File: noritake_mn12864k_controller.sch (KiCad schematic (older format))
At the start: 43 parts, among them J1 Conn_01x11, J2 USB_C_Receptacle_USB2.0, J3 TagConnect_TC2030_SWD, Q1 AO3400A, Q2 AO3400A, T1 Wuerth 760390013, U1 MN12864K, U2 74HC14, U3 CD4051B, U4 SN74AVC8T245PW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

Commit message: Connect shutdown and ifsel
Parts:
- removed C12, C3, C4: 100nF, Capacitor_SMD:C_0402_1005Metric, symbol Device:C
- removed C24: 10uF, Capacitor_SMD:C_1206_3216Metric, symbol Device:C
- removed C25: 4.7uF, Capacitor_SMD:C_1206_3216Metric, symbol Device:C
- removed C?: 1uF, Capacitor_SMD:C_0402_1005Metric, symbol Device:C
- removed D1: 5V6, Diode_SMD:D_MiniMELF, symbol Device:D_Zener
- removed Q1, Q2: AO3400A, Package_TO_SOT_SMD:SOT-23, symbol Transistor_FET:AO3400A
- removed R5: 22R, Resistor_SMD:R_1206_3216Metric, symbol Device:R
- removed R7: 10kR, Resistor_SMD:R_1206_3216Metric, symbol Device:R
- removed T1: Wuerth 760390013, Transformer_Würth:Transformer_Würth_10.05x6.73_6P, symbol Transformer_Isolation:Transformer_SP_SS
- removed U1: MN12864K, VFD_Noritake:MN12864K, symbol VFD_Noritake:MN12864K
- removed U4: SN74AVC8T245PW, Package_SO:TSSOP-24_4.4x7.8mm_P0.65mm, symbol Logic_LevelTranslator:SN74AVC8T245PW
- added H1, H2: ToolingHole, ToolingHole:ToolingHole_JLCSMT, symbol Mechanical:MountingHole
- added H3, H4: MountingHole, MountingHole:MountingHole_2.7mm_M2.5, symbol Mechanical:MountingHole
- added R? (x4): 100kR, Resistor_SMD:R_0402_1005Metric, symbol Device:R
- added TP1: DEBUG00, TestPoint:TestPoint_Pad_D2.0mm, symbol Connector:TestPoint
- added TP?: DEBUG01, TestPoint:TestPoint_Pad_D2.0mm, symbol Connector:TestPoint
- added TP?: DEBUG02, TestPoint:TestPoint_Pad_D2.0mm, symbol Connector:TestPoint
- added TP?: DEBUG03, TestPoint:TestPoint_Pad_D2.0mm, symbol Connector:TestPoint
- added TP?: DEBUG04, TestPoint:TestPoint_Pad_D2.0mm, symbol Connector:TestPoint
- added TP?: DEBUG05, TestPoint:TestPoint_Pad_D2.0mm, symbol Connector:TestPoint
- added TP?: DEBUG06, TestPoint:TestPoint_Pad_D2.0mm, symbol Connector:TestPoint
- added TP?: DEBUG07, TestPoint:TestPoint_Pad_D2.0mm, symbol Connector:TestPoint
- added TP?: DEBUG08, TestPoint:TestPoint_Pad_D2.0mm, symbol Connector:TestPoint
- added TP?: DEBUG09, TestPoint:TestPoint_Pad_D2.0mm, symbol Connector:TestPoint
- added TP?: DEBUG10, TestPoint:TestPoint_Pad_D2.0mm, symbol Connector:TestPoint
- added TP?: DEBUG11, TestPoint:TestPoint_Pad_D2.0mm, symbol Connector:TestPoint
- added TP?: DEBUG12, TestPoint:TestPoint_Pad_D2.0mm, symbol Connector:TestPoint
- added TP?: DEBUG13, TestPoint:TestPoint_Pad_D2.0mm, symbol Connector:TestPoint
- added TP?: DEBUG14, TestPoint:TestPoint_Pad_D2.0mm, symbol Connector:TestPoint
- added TP?: DEBUG15, TestPoint:TestPoint_Pad_D2.0mm, symbol Connector:TestPoint
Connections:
- net +3V3: now also R?.1, R?.1, R?.2, R?.2
- net CPOL: now also J1.3 (Pin_3); no longer J1.5 (Pin_5)
- net IFSEL: now also U5.56 (PB4), R?.1
- net VFD_BLK: now also U5.25 (PB0); no longer U5.50 (PA15)
- net VFD_GSBLK: now also U5.26 (PB1); no longer U5.42 (PA9)
- net VFD_LAT: now also U5.42 (PA9); no longer U5.41 (PA8)
- net ~CS: now also R?.2
- net ~RST: now also J1.5 (Pin_5), R?.2; no longer J1.3 (Pin_3)
- net ~SHDWN: now also U5.58 (PB6), R?.1
- net DBG08: now reaches U5.10 (PC2)
- net DBG08: now also TP?.1
- net DBG09: now reaches U5.11 (PC3)
- net DBG09: now also TP?.1
- net DBG10: now reaches U5.24 (PC4)
- net DBG10: now also TP?.1
- net DBG05: now reaches U5.27 (PB2)
- net DBG05: now also TP?.1
- net DBG01: now reaches U5.28 (PB10)
- net DBG01: now also TP?.1
- net DBG02: now reaches U5.29 (PB11)
- net DBG02: now also TP?.1
- net DBG03: now reaches U5.33 (PB12)
- net DBG03: now also TP?.1
- net DBG04: now reaches U5.35 (PB14)
- net DBG04: now also TP?.1
- net DBG11: now reaches U5.37 (PC6)
- net DBG11: now also TP?.1
- net DBG12: now reaches U5.38 (PC7)
- net DBG12: now also TP?.1
- net DBG13: now reaches U5.39 (PC8)
- net DBG13: now also TP?.1
- net DBG14: now reaches U5.40 (PC9)
- net DBG14: now also TP?.1
- net VFD_HTR_G2: now reaches U5.43 (PA10)
- net DBG15: now reaches U5.51 (PC10)
- net DBG15: now also TP?.1
- net DBG00: now reaches U5.62 (PB9)
- net DBG00: now also TP1.1
- net DBG06: now reaches U5.8 (PC0)
- net DBG06: now also TP?.1
- net DBG07: now reaches U5.9 (PC1)
- net DBG07: now also TP?.1
- new net VFD_HTR_G1: U5.41 (PA8)
- new net VFD_HV_EN: U5.50 (PA15)
- no-connect marks 8 -> 7
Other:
- moved on the sheet: C15, C16, C17, C19, C20, C22, C23, J3, JP1, R6, U5

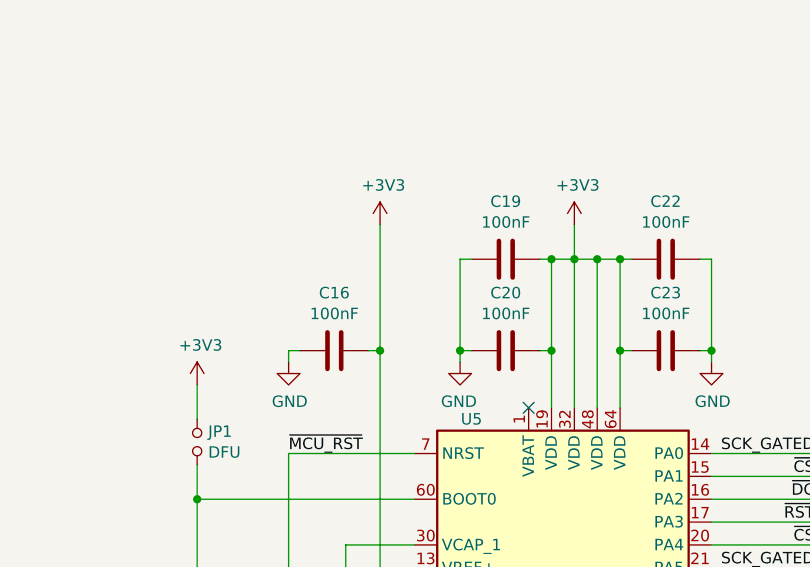
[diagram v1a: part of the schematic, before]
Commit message: Add dual filament transformer option
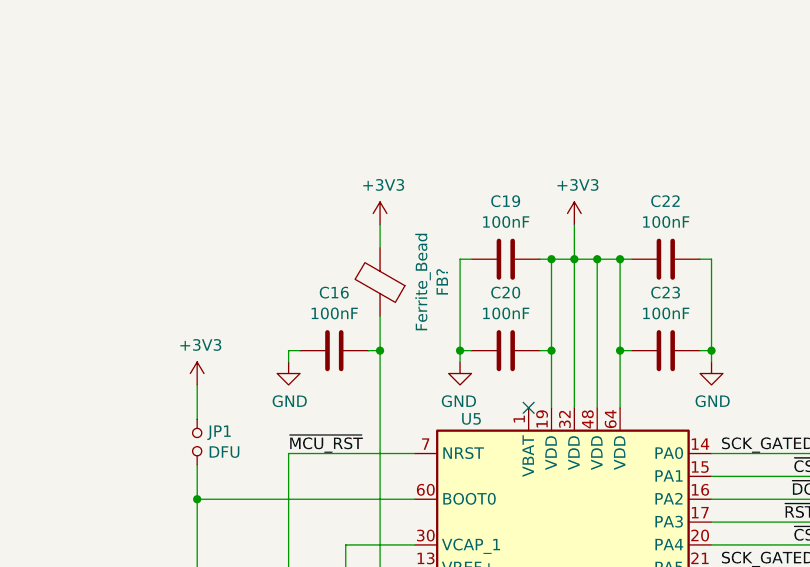
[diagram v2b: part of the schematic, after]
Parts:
- added FB?: Ferrite_Bead, Inductor_SMD:L_0805_2012Metric, symbol Device:Ferrite_Bead
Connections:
- net +3V3: now also FB?.2; no longer C16.2, U5.13 (VREF+)
- new net: C16.2, FB?.1, U5.13 (VREF+)
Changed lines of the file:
@@
 Wire Wire Line
 	14850 4000 14900 4000
-Connection ~ 14900 4000
-Wire Wire Line
-	14900 4000 14900 3450
 Wire Wire Line
 	15050 4850 14750 4850
@@
 Text Label 16800 6750 2    50   ~ 0
 ~SHDWN
+$Comp
+L Device:Ferrite_Bead FB?
+U 1 1 61290FB4
+P 14900 3700
+F 0 "FB?" V 14626 3700 50  0000 C CNN
+F 1 "Ferrite_Bead" V 14717 3700 50  0000 C CNN
+F 2 "Inductor_SMD:L_0805_2012Metric" V 14830 3700 50  0001 C CNN
+F 3 "~" H 14900 3700 50  0001 C CNN
+F 4 "C1015" V 14900 3700 50  0001 C CNN "LCSC"
+	1    14900 3700
+	-1   0    0    1
+$EndComp
+Wire Wire Line
+	14900 3850 14900 4000
+Connection ~ 14900 4000
+Wire Wire Line
+	14900 3550 14900 3450
 $EndSCHEMATC

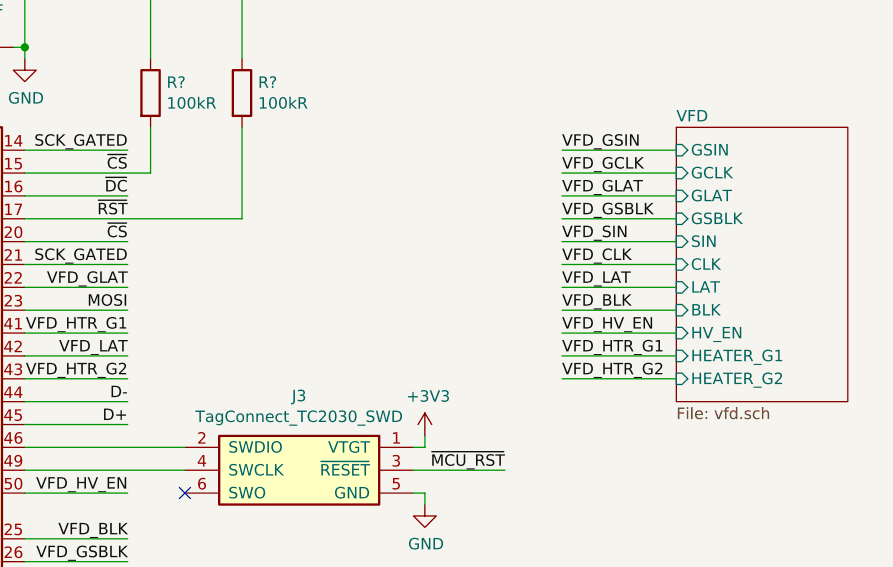
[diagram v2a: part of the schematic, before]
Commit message: Add PA4/PA5 5V todo
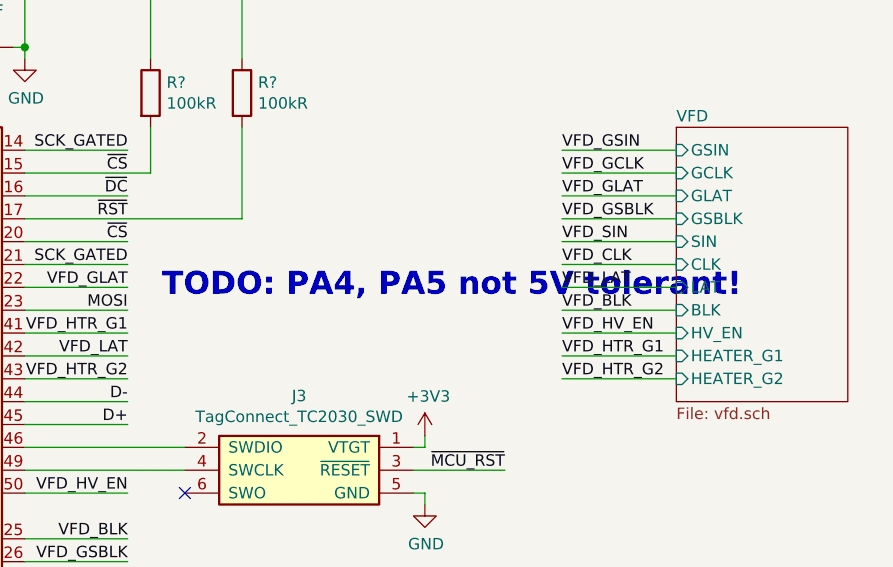
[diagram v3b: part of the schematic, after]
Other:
- note added: "TODO: PA4, PA5 not 5V tolerant!"
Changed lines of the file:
@@
 Wire Wire Line
 	14900 3550 14900 3450
+Text Notes 16950 5100 0    100  ~ 20
+TODO: PA4, PA5 not 5V tolerant!
 $EndSCHEMATC

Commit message: Add VFD section
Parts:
- added C31, C34: 100nF, Capacitor_SMD:C_0402_1005Metric, symbol Device:C
- added R27, R28: 100kR, Resistor_SMD:R_0402_1005Metric, symbol Device:R
- added R29: 5.1kR, Resistor_SMD:R_0402_1005Metric, symbol Device:R
- gave numbers to parts that had none: 20
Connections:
- net VFD_HV_EN is gone; now on net ~CS: U5.50 (PA15)
- net +3V3: now also R27.2, R28.2
- net 4WIRE: now also R27.1
- net CPOL: now also R28.1
- net DBG00: now also U5.26 (PB1); no longer U5.62 (PB9)
- net DBG01: now also U5.62 (PB9); no longer U5.28 (PB10)
- net DBG02: now also U5.28 (PB10); no longer U5.29 (PB11)
- net DBG03: now also U5.29 (PB11); no longer U5.33 (PB12)
- net DBG04: now also U5.33 (PB12); no longer U5.35 (PB14)
- net DBG05: now also U5.35 (PB14); no longer U5.27 (PB2)
- net DBG06: now also U5.27 (PB2); no longer U5.8 (PC0)
- net DBG07: now also U5.8 (PC0); no longer U5.9 (PC1)
- net DBG08: now also U5.9 (PC1); no longer U5.10 (PC2)
- net DBG09: now also U5.10 (PC2); no longer U5.11 (PC3)
- net DBG10: now also U5.11 (PC3); no longer U5.24 (PC4)
- net DBG11: now also U5.24 (PC4); no longer U5.37 (PC6)
- net DBG12: now also U5.37 (PC6); no longer U5.38 (PC7)
- net DBG13: now also U5.38 (PC7); no longer U5.39 (PC8)
- net DBG14: now also U5.39 (PC8); no longer U5.40 (PC9)
- net DBG15: now also U5.40 (PC9); no longer U5.51 (PC10)
- net GND: now also C31.1, C34.1
- net SCK_GATED: now also U5.55 (PB3); no longer U5.21 (PA5)
- net VFD_BLK: now also U5.20 (PA4); no longer U5.25 (PB0)
- net VFD_GCLK: now also U5.51 (PC10); no longer U5.55 (PB3)
- net VFD_GSBLK: now also U5.21 (PA5); no longer U5.26 (PB1)
- net ~CS: no longer U5.20 (PA4)
- net VFD_HV_G: now reaches U5.52 (PC11)
- new net VFD/STEPUP_FB: C31.2, R29.2
- new net VFD_HV_FB: C34.2, R29.1, U5.25 (PB0)
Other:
- note removed: "TODO: PA4, PA5 not 5V tolerant!"
- moved on the sheet: C1, C10, C13, C14, C18, C21, FB2, TP1, TP10, TP11, TP12, TP13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

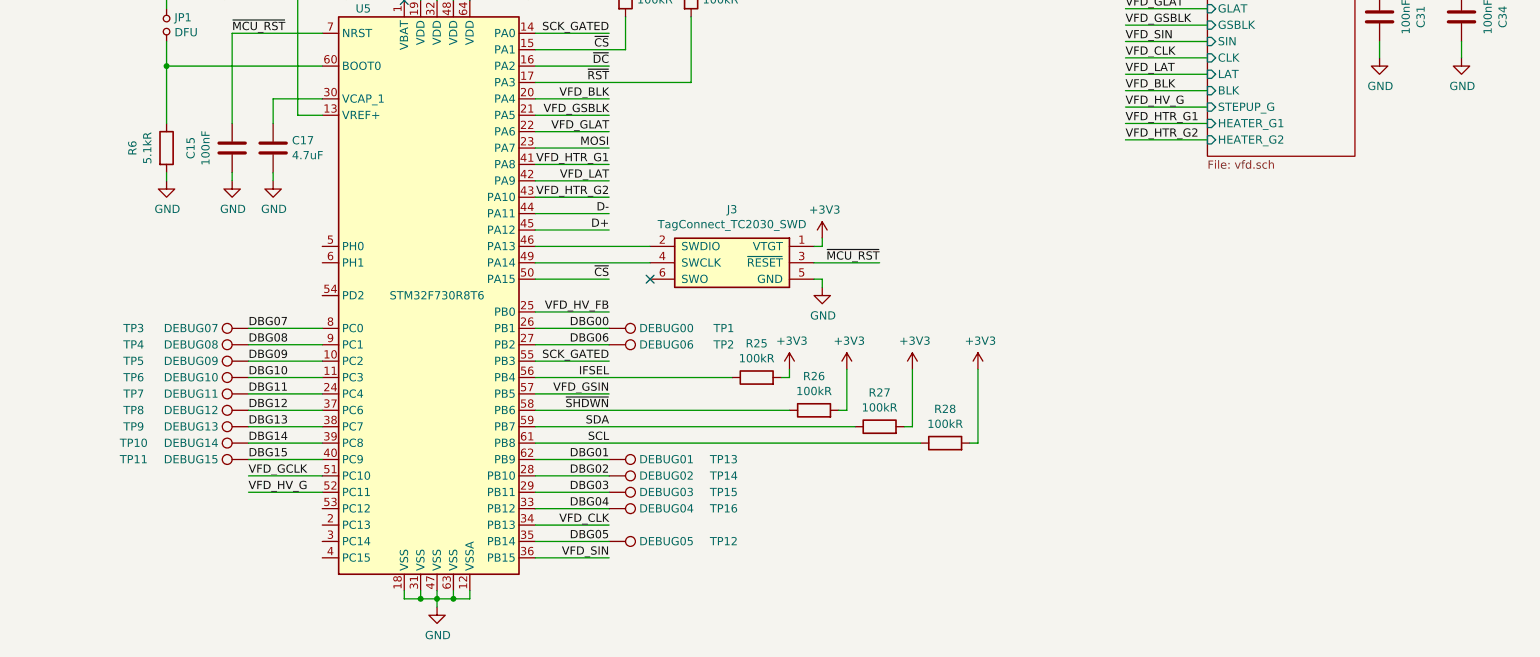
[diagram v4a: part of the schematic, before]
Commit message: Fix grid protection
Ensure only edges are detected
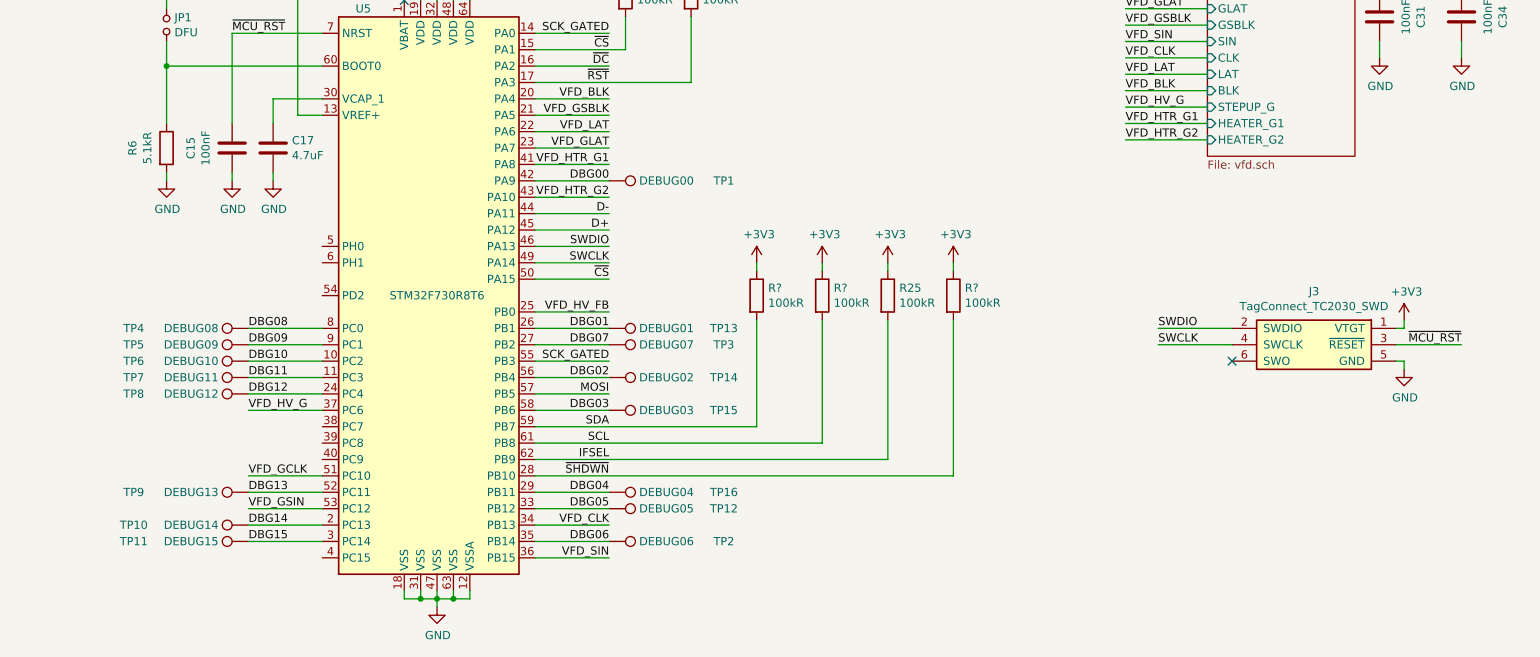
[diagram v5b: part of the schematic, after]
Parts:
- removed R26, R27, R28: 100kR, Resistor_SMD:R_0402_1005Metric, symbol Device:R
- added R? (x3): 100kR, Resistor_SMD:R_0402_1005Metric, symbol Device:R
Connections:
- net +3V3: now also R25.1, R?.1, R?.1, R?.1; no longer R25.2
- net 4WIRE: now also R?.2
- net CPOL: now also R?.2
- net DBG00: now also U5.42 (PA9); no longer U5.26 (PB1)
- net DBG01: now also U5.26 (PB1); no longer U5.62 (PB9)
- net DBG02: now also U5.56 (PB4); no longer U5.28 (PB10)
- net DBG03: now also U5.58 (PB6); no longer U5.29 (PB11)
- net DBG04: now also U5.29 (PB11); no longer U5.33 (PB12)
- net DBG05: now also U5.33 (PB12); no longer U5.35 (PB14)
- net DBG06: now also U5.35 (PB14); no longer U5.27 (PB2)
- net DBG07: now also U5.27 (PB2); no longer U5.8 (PC0)
- net DBG08: now also U5.8 (PC0); no longer U5.9 (PC1)
- net DBG09: now also U5.9 (PC1); no longer U5.10 (PC2)
- net DBG10: now also U5.10 (PC2); no longer U5.11 (PC3)
- net DBG11: now also U5.11 (PC3); no longer U5.24 (PC4)
- net DBG12: now also U5.24 (PC4); no longer U5.37 (PC6)
- net DBG13: now also U5.52 (PC11); no longer U5.38 (PC7)
- net DBG14: now also U5.2 (PC13); no longer U5.39 (PC8)
- net DBG15: now also U5.3 (PC14); no longer U5.40 (PC9)
- net IFSEL: now also R25.2, U5.62 (PB9); no longer R25.1, U5.56 (PB4)
- net MOSI: now also U5.57 (PB5); no longer U5.23 (PA7)
- net VFD_GLAT: now also U5.23 (PA7); no longer U5.22 (PA6)
- net VFD_GSIN: now also U5.53 (PC12); no longer U5.57 (PB5)
- net VFD_HV_G: now also U5.37 (PC6); no longer U5.52 (PC11)
- net VFD_LAT: now also U5.22 (PA6); no longer U5.42 (PA9)
- net ~SHDWN: now also U5.28 (PB10), R?.2; no longer U5.58 (PB6)
- net SWDIO: now reaches J3.2 (SWDIO), U5.46 (PA13)
- net SWCLK: now reaches J3.4 (SWCLK), U5.49 (PA14)
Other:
- moved on the sheet: J3, R25, TP1, TP10, TP11, TP12, TP13, TP14, TP15, TP16, TP2, TP3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

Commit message: Complete intra section layout
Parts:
- added J4: Conn_01x18, Connector_FFC:MINTRON-LW05202-18, symbol Connector_Generic_MountingPin:Conn_01x18_MountingPin
- added U10, U11, U12: SRV05-4, Package_TO_SOT_SMD:SOT-23-6, symbol Power_Protection:SRV05-4
- gave numbers to parts that had none: 3
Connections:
- net +5V: now also U10.5 (VP), U11.5 (VP), U12.5 (VP)
- net 4WIRE: now also U10.3 (IO2)
- net CPOL: now also U10.1 (IO1)
- net DBG00: now also J4.2 (Pin_2)
- net DBG01: now also J4.3 (Pin_3)
- net DBG02: now also J4.4 (Pin_4)
- net DBG03: now also J4.5 (Pin_5)
- net DBG04: now also J4.6 (Pin_6)
- net DBG05: now also J4.7 (Pin_7)
- net DBG06: now also J4.8 (Pin_8)
- net DBG07: now also J4.9 (Pin_9)
- net DBG08: now also J4.10 (Pin_10)
- net DBG09: now also J4.11 (Pin_11)
- net DBG10: now also J4.12 (Pin_12)
- net DBG11: now also J4.13 (Pin_13)
- net DBG12: now also J4.14 (Pin_14)
- net DBG13: now also J4.15 (Pin_15)
- net DBG14: now also J4.16 (Pin_16)
- net DBG15: now also J4.17 (Pin_17)
- net GND: now also J4.1 (Pin_1), J4.18 (Pin_18), J4.MP (MountPin), U10.2 (VN), U11.2 (VN), U12.2 (VN)
- net IFSEL: now also U11.6 (IO4)
- net MOSI: now also U11.3 (IO2)
- net SCK: now also U11.4 (IO3)
- net ~CS: now also U11.1 (IO1)
- net ~DC: now also U10.6 (IO4)
- net ~RST: now also U10.4 (IO3)
- net ~SHDWN: now also U12.1 (IO1)
- no-connect marks 7 -> 10

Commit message: Add missing LCSC partnumbers
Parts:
- U10, U11, U12, U8: LCSC (none) -> C85364
- U5: LCSC (none) -> C478453
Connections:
- net CPOL: now also U2.1; no longer U2.5
- net ~CS: now also U2.5; no longer U2.1
- net at U2.2: now also U3.9 (C); no longer U3.11 (A)
- net at U2.6: now also U3.11 (A); no longer U3.9 (C)
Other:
- moved on the sheet: U2A, U2C
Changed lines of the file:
@@
 F 2 "Package_QFP:LQFP-64_10x10mm_P0.5mm" H 15150 4350 50  0001 R CNN
 F 3 "http://www.st.com/st-web-ui/static/active/en/resource/technical/document/datasheet/DM00330506.pdf" H 15750 6050 50  0001 C CNN
+F 4 "C478453" H 15750 6050 50  0001 C CNN "LCSC"
 	1    15750 6050
 	1    0    0    -1
@@
 F 2 "Package_TO_SOT_SMD:SOT-23-6" H 3700 3100 50  0001 C CNN
 F 3 "http://www.onsemi.com/pub/Collateral/SRV05-4-D.PDF" H 3000 3550 50  0001 C CNN
+F 4 "C85364" H 3000 3550 50  0001 C CNN "LCSC"
 	1    3000 3550
 	1    0    0    -1
@@
 L 74xx:74HC14 U2
 U 3 1 5FAE5E1C
-P 1300 7500
-F 0 "U2" H 1300 7817 50  0000 C CNN
-F 1 "74HC14" H 1300 7726 50  0000 C CNN
-F 2 "Package_SO:SOIC-14_3.9x8.7mm_P1.27mm" H 1300 7500 50  0001 C CNN
-F 3 "http://www.ti.com/lit/gpn/sn74LS08" H 1300 7500 50  0001 C CNN
-F 4 "C5605" H 1300 7500 50  0001 C CNN "LCSC"
-	3    1300 7500
+P 1300 6500
+F 0 "U2" H 1300 6817 50  0000 C CNN
+F 1 "74HC14" H 1300 6726 50  0000 C CNN
+F 2 "Package_SO:SOIC-14_3.9x8.7mm_P1.27mm" H 1300 6500 50  0001 C CNN
+F 3 "http://www.ti.com/lit/gpn/sn74LS08" H 1300 6500 50  0001 C CNN
+F 4 "C5605" H 1300 6500 50  0001 C CNN "LCSC"
+	3    1300 6500
 	1    0    0    -1
 $EndComp
@@
 L 74xx:74HC14 U2
 U 1 1 5FADB1D7
-P 1300 6500
-F 0 "U2" H 1300 6817 50  0000 C CNN
-F 1 "74HC14" H 1300 6726 50  0000 C CNN
-F 2 "Package_SO:SOIC-14_3.9x8.7mm_P1.27mm" H 1300 6500 50  0001 C CNN
-F 3 "http://www.ti.com/lit/gpn/sn74LS08" H 1300 6500 50  0001 C CNN
-F 4 "C5605" H 1300 6500 50  0001 C CNN "LCSC"
-	1    1300 6500
+P 1300 7500
+F 0 "U2" H 1300 7817 50  0000 C CNN
+F 1 "74HC14" H 1300 7726 50  0000 C CNN
+F 2 "Package_SO:SOIC-14_3.9x8.7mm_P1.27mm" H 1300 7500 50  0001 C CNN
+F 3 "http://www.ti.com/lit/gpn/sn74LS08" H 1300 7500 50  0001 C CNN
+F 4 "C5605" H 1300 7500 50  0001 C CNN "LCSC"
+	1    1300 7500
 	1    0    0    -1
 $EndComp
@@
 F 2 "Package_TO_SOT_SMD:SOT-23-6" H 7550 1700 50  0001 C CNN
 F 3 "http://www.onsemi.com/pub/Collateral/SRV05-4-D.PDF" H 6850 2150 50  0001 C CNN
+F 4 "C85364" H 6850 2150 50  0001 C CNN "LCSC"
 	1    6850 2150
 	1    0    0    -1
@@
 F 2 "Package_TO_SOT_SMD:SOT-23-6" H 9050 1700 50  0001 C CNN
 F 3 "http://www.onsemi.com/pub/Collateral/SRV05-4-D.PDF" H 8350 2150 50  0001 C CNN
+F 4 "C85364" H 8350 2150 50  0001 C CNN "LCSC"
 	1    8350 2150
 	1    0    0    -1
@@
 F 2 "Package_TO_SOT_SMD:SOT-23-6" H 10650 1700 50  0001 C CNN
 F 3 "http://www.onsemi.com/pub/Collateral/SRV05-4-D.PDF" H 9950 2150 50  0001 C CNN
+F 4 "C85364" H 9950 2150 50  0001 C CNN "LCSC"
 	1    9950 2150
 	1    0    0    -1
